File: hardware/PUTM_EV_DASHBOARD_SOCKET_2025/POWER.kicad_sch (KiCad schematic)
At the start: 10 parts, among them J4 Conn_01x01, J5 Conn_01x01, J5POWER1 Conn_01x06_MountingPin, J8 Conn_01x03_Socket, U1 SPX3819M5-L-5-0, U2 SPX3819M5-L-3-3

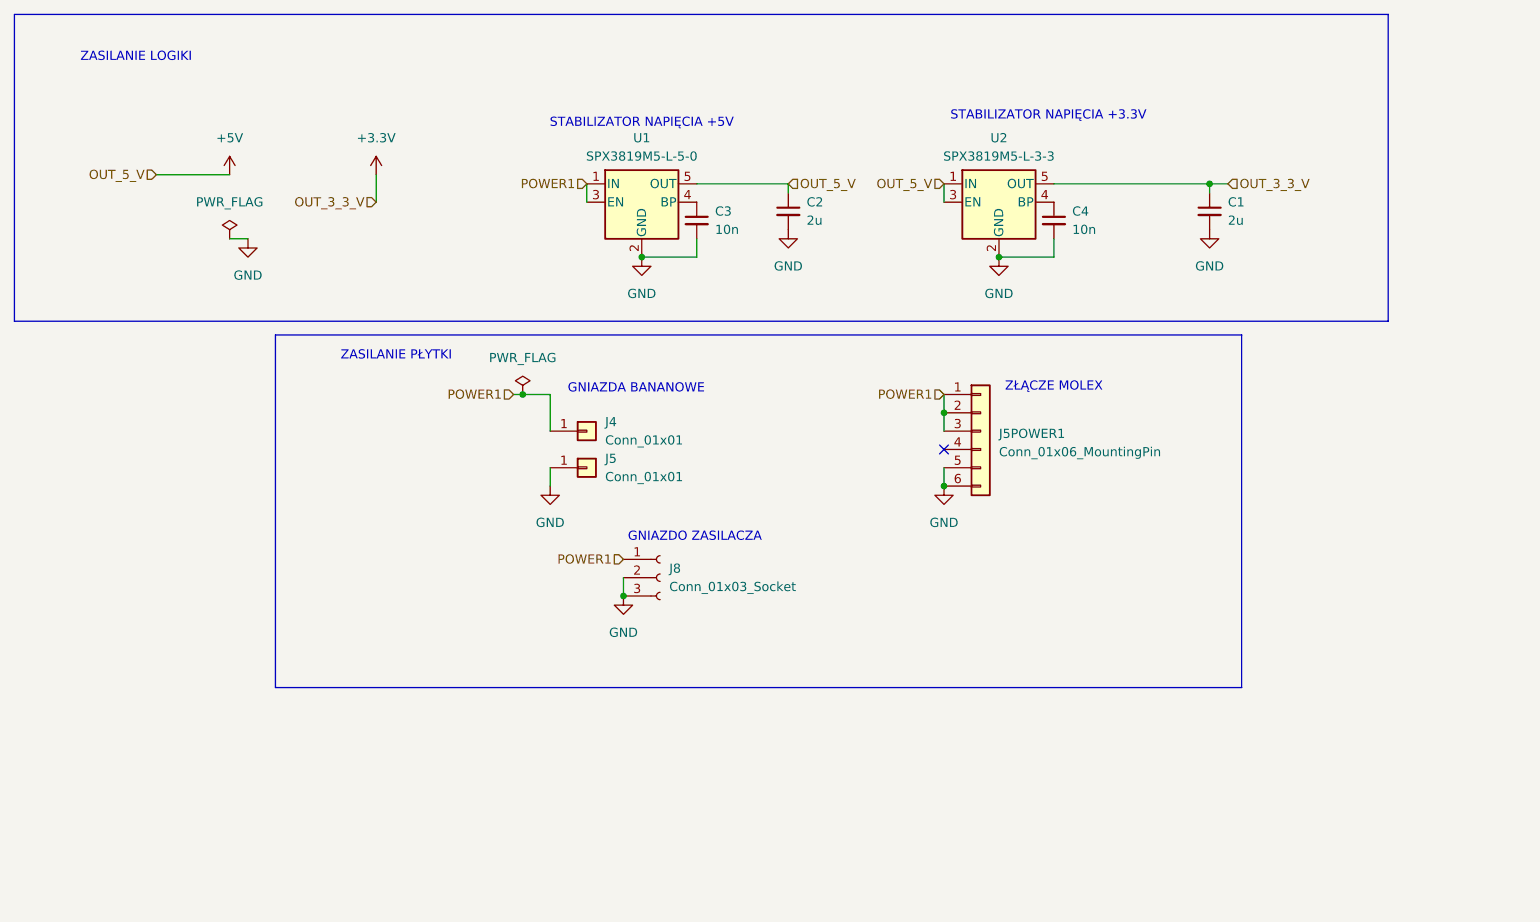
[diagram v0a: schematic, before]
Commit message: dodano łezki do pól smd, pola lutownicze do przelotek, dodano zabezpieczenie przed odwrotna polaryzacją, odsunięto ścieżki od krawędzi płytki, poprawiono can,
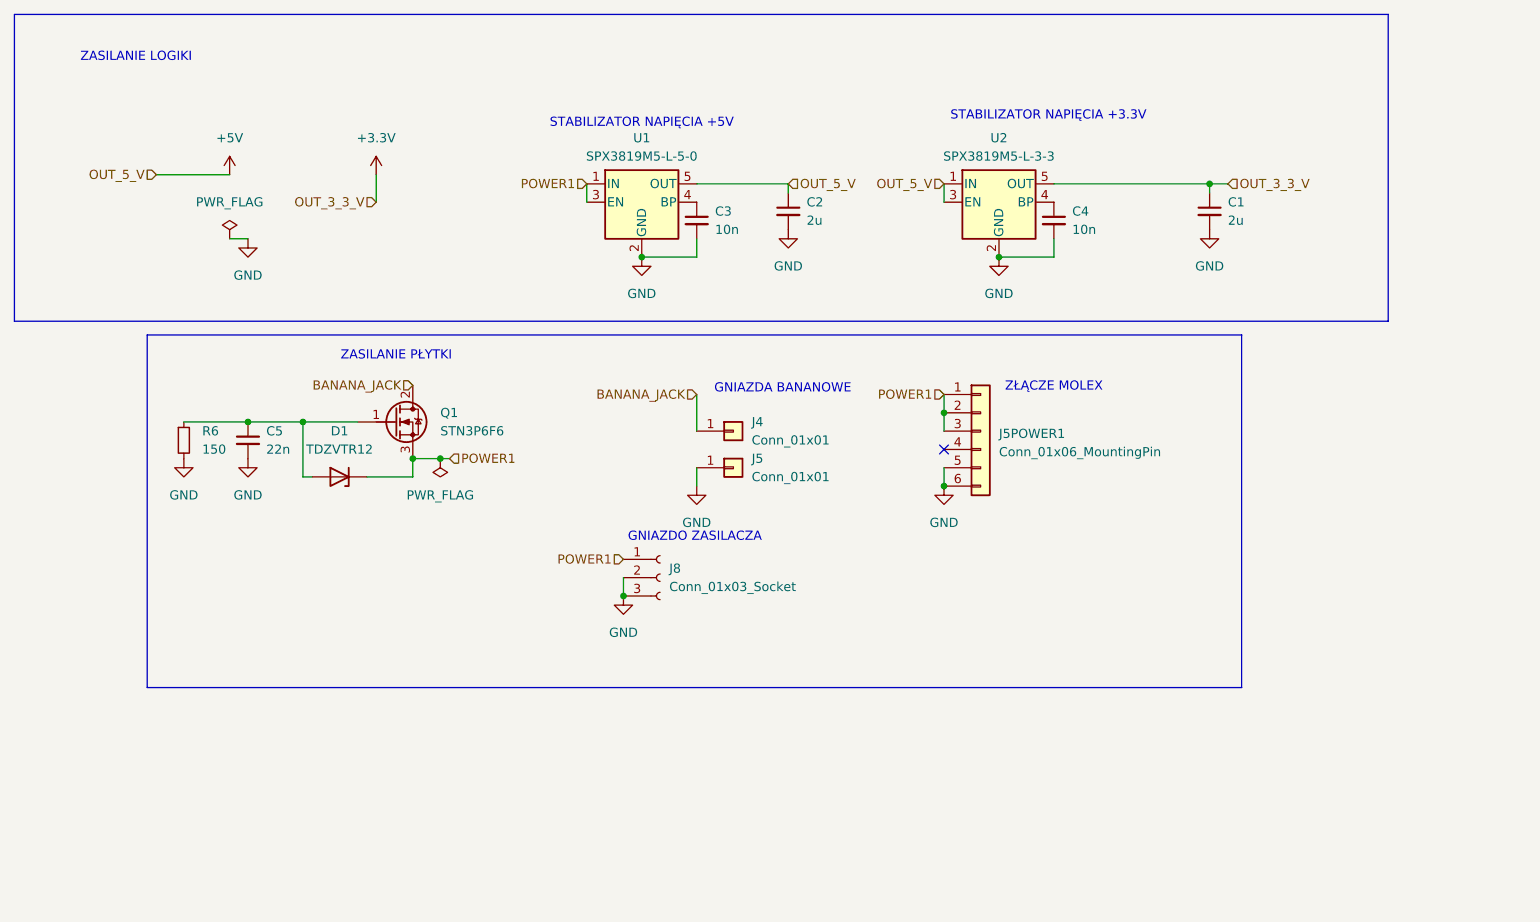
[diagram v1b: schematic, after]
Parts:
- added C5: 22n, Capacitor_SMD:C_0603_1608Metric, symbol Device:C_Small
- added D1: TDZVTR12, SamacSys_Parts:TDZVTR20, symbol Device:D_Zener
- added Q1: STN3P6F6, Package_TO_SOT_SMD:SOT-223-3_TabPin2, symbol Transistor_FET:BSP129
- added R6: 150, Resistor_SMD:R_1206_3216Metric, symbol Device:R_Small
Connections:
- net GND: now also C5.2, R6.2
- net POWER1: now also D1.1 (K), Q1.3 (S); no longer J4.1 (Pin_1)
- new net: C5.1, D1.2 (A), Q1.1 (G), R6.1
- new net BANANA_JACK: J4.1 (Pin_1), Q1.2 (D)
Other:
- moved on the sheet: J4, J5

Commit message: Bogracz Czas przygotowania: 3 godziny 30 minut Liczba porcji: 2100 g gulaszu  W 100 g dania: Wartość energetyczna 156 kcal Węglowodany 5 g - W tym cukry 2 g Białko 7 g Tłuszcze 12 g
Składniki

800 g mięsa wołowego - np. pręga oraz łopatka
200 g boczku gotowanego wędzonego
100 g dobrej jakosci słoniny
6 łyżek dobrej jakości smalcu - około 100 g
2 średniej wielkości cebule - około 330 g
2 średniej wielkości czerwone papryki - około 400 g
5 ząbków czosnku - około 25 g
500 g ziemniaków - można pominąć lub dać kluseczki
2 łyżki koncentratu pomidorowego - do 50 g
400 ml wody - trochę więcej niż 1,5 szklanki
zioła i przyprawy: 2 listki laurowe, 3 ziarna ziela angielskiego; 1 pełna łyżeczka słodkiej papryki; 1 płaska łyżeczka soli; po pół łyżeczki wędzonej i ostrej papryki; 1/3 łyżeczki czarnego pieprzu
Składniki:
Bogracz
Szklanka ma u mnie pojemność 250 ml.

Warzywa ważone były przed ewentualnym obraniem/przygotowaniem. Zawsze podaję wagę użytych przeze mnie warzyw lub owoców. Nie trzeba jednak stosować się do wytycznych co do grama. Wagi podawane są po to, by łatwiej Wam było zorientować się, jaka mniej więcej ilość potrzebna jest do zrobienia danego dania.

Kalorie policzone zostały na podstawie użytych przeze mnie składników. Jest to więc orientacyjna liczba kalorii, ponieważ Twoje składniki mogą mieć inną liczbę kalorii niż te, których użyłam ja. Z podanej ilości składników otrzymasz Bogracz o wadze około 2100 gramów. Zanim zaczniesz szykować ten gulasz, polecam najpierw przeczytać cały przepis, by przygotować się odpowiednio wcześniej do kolejnych etapów wykonania.

UWAGA: Bogracz, to rodzaj kociołka stalowego lub emaliowanego, który rozszerza się ku górze. Kociołek podwieszany jest na trójnogu i wieszany na metalowym łańcuchu. Bogracz wisi nad ogniskiem, a w środku gotuje się węgierski gulasz. Zaczęto zatem nazywać tak samo i danie. Ponieważ zdecydowana większość Czytelników nie ma możliwości szykowania tego gulaszu w kociołku na świeżym powietrzu, podaję przepis na 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
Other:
- note added: "ZABEZPIECZENIE PRZED ODWROTNĄ POLARYZACJĄ"
- moved on the sheet: C5, D1, Q1, R6
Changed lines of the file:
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@@
+		)
+	)
+	(text "ZABEZPIECZENIE PRZED ODWROTNĄ POLARYZACJĄ\n"
+		(exclude_from_sim no)
+		(at 82.55 72.644 0)
+		(effects
+			(font
+				(size 1.27 1.27)
+			)
 		)
 	)
@@
 	)
 	(junction
-		(at 92.71 77.47)
+		(at 93.98 87.63)
 		(diameter 0)
 		(color 0 0 0 0)
@@
 	)
 	(junction
-		(at 69.85 72.39)
+		(at 71.12 82.55)
 		(diameter 0)
 		(color 0 0 0 0)
@@
 	)
 	(junction
-		(at 77.47 72.39)
+		(at 78.74 82.55)
 		(diameter 0)
 		(color 0 0 0 0)
 	)
 	(junction
-		(at 96.52 77.47)
+		(at 97.79 87.63)
 		(diameter 0)
 		(color 0 0 0 0)
@@
 	(wire
 		(pts
-			(xy 77.47 72.39) (xy 85.09 72.39)
+			(xy 78.74 82.55) (xy 86.36 82.55)
 		)
 		(stroke
@@
 	(wire
 		(pts
-			(xy 77.47 80.01) (xy 77.47 72.39)
+			(xy 78.74 90.17) (xy 78.74 82.55)
 		)
 		(stroke
@@
 	(wire
 		(pts
-			(xy 92.71 80.01) (xy 92.71 77.47)
+			(xy 93.98 90.17) (xy 93.98 87.63)
 		)
 		(stroke
@@
 	(wire
 		(pts
-			(xy 97.79 77.47) (xy 96.52 77.47)
+			(xy 99.06 87.63) (xy 97.79 87.63)
 		)
 		(stroke
@@
 	(wire
 		(pts
-			(xy 96.52 77.47) (xy 92.71 77.47)
+			(xy 97.79 87.63) (xy 93.98 87.63)
 		)
 		(stroke
@@
 	(wire
 		(pts
-			(xy 69.85 72.39) (xy 77.47 72.39)
+			(xy 71.12 82.55) (xy 78.74 82.55)
 		)
 		(stroke
@@
 	(wire
 		(pts
-			(xy 86.36 80.01) (xy 92.71 80.01)
+			(xy 87.63 90.17) (xy 93.98 90.17)
 		)
 		(stroke
@@
 	(wire
 		(pts
-			(xy 78.74 80.01) (xy 77.47 80.01)
+			(xy 80.01 90.17) (xy 78.74 90.17)
 		)
 		(stroke
@@
 	(wire
 		(pts
-			(xy 60.96 72.39) (xy 69.85 72.39)
+			(xy 62.23 82.55) (xy 71.12 82.55)
 		)
 		(stroke
@@
 	(hierarchical_label "BANANA_JACK"
 		(shape input)
-		(at 92.71 67.31 180)
+		(at 93.98 77.47 180)
 		(effects
 			(font
@@
 	(hierarchical_label "POWER1"
 		(shape input)
-		(at 97.79 77.47 0)
+		(at 99.06 87.63 0)
 		(effects
 			(font
@@
 	(symbol
 		(lib_id "Device:C_Small")
-		(at 69.85 74.93 0)
+		(at 71.12 85.09 0)
 		(unit 1)
 		(exclude_from_sim no)
@@
 		(fields_autoplaced yes)
 		(property "Reference" "C5"
-			(at 72.39 73.6662 0)
+			(at 73.66 83.8262 0)
 			(effects
 				(font
@@
 		)
 		(property "Value" "22n"
-			(at 72.39 76.2062 0)
+			(at 73.66 86.3662 0)
 			(effects
 				(font
@@
 		)
 		(property "Footprint" "Capacitor_SMD:C_0603_1608Metric"
-			(at 69.85 74.93 0)
+			(at 71.12 85.09 0)
 			(effects
 				(font
@@
 		)
 		(property "Datasheet" "~"
-			(at 69.85 74.93 0)
+			(at 71.12 85.09 0)
 			(effects
 				(font
@@
 		)
 		(property "Description" "Unpolarized capacitor, small symbol"
-			(at 69.85 74.93 0)
+			(at 71.12 85.09 0)
 			(effects
 				(font
@@
 	(symbol
 		(lib_id "Device:R_Small")
-		(at 60.96 74.93 0)
+		(at 62.23 85.09 0)
 		(unit 1)
 		(exclude_from_sim no)
@@
 		(dnp no)
 		(property "Reference" "R6"
-			(at 63.5 73.6599 0)
+			(at 64.77 83.8199 0)
 			(effects
 				(font
@@
 		)
 		(property "Value" "150"
-			(at 63.5 76.1999 0)
+			(at 64.77 86.3599 0)
 			(effects
 				(font
@@
 		)
 		(property "Footprint" "Resistor_SMD:R_1206_3216Metric"
-			(at 60.96 74.93 0)
+			(at 62.23 85.09 0)
 			(effects
 				(font
@@
 		)
 		(property "Datasheet" "~"
-			(at 60.96 74.93 0)
+			(at 62.23 85.09 0)
 			(effects
 				(font
@@
 		)
 		(property "Description" "Resistor, small symbol"
-			(at 60.96 74.93 0)
+			(at 62.23 85.09 0)
 			(effects
 				(font
@@
 	(symbol
 		(lib_id "Device:D_Zener")
-		(at 82.55 80.01 180)
+		(at 83.82 90.17 180)
 		(unit 1)
 		(exclude_from_sim no)
@@
 		(dnp no)
 		(property "Reference" "D1"
-			(at 82.55 73.66 0)
+			(at 83.82 83.82 0)
 			(effects
 				(font
@@
 		)
 		(property "Value" "TDZVTR12"
-			(at 82.55 76.2 0)
+			(at 83.82 86.36 0)
 			(effects
 				(font
@@
 		)
 		(property "Footprint" "SamacSys_Parts:TDZVTR20"
-			(at 82.55 80.01 0)
+			(at 83.82 90.17 0)
 			(effects
 				(font
@@
 		)
 		(property "Datasheet" "https://www.mouser.pl/ProductDetail/ROHM-Semiconductor/TDZVTR12?qs=4v%252BiZTmLVHH4uFenhw55Ug%3D%3D"
-			(at 82.55 80.01 0)
+			(at 83.82 90.17 0)
 			(effects
 				(font
@@
 		)
 		(property "Description" "Zener diode"
-			(at 82.55 80.01 0)
+			(at 83.82 90.17 0)
 			(effects
 				(font
@@
 	(symbol
 		(lib_id "Transistor_FET:BSP129")
-		(at 90.17 72.39 0)
+		(at 91.44 82.55 0)
 		(unit 1)
 		(exclude_from_sim no)
@@
 		(fields_autoplaced yes)
 		(property "Reference" "Q1"
-			(at 96.52 71.1199 0)
+			(at 97.79 81.2799 0)
 			(effects
 				(font
@@
 		)
 		(property "Value" "STN3P6F6"
-			(at 96.52 73.6599 0)
+			(at 97.79 83.8199 0)
 			(effects
 				(font
@@
 		)
 		(property "Footprint" "Package_TO_SOT_SMD:SOT-223-3_TabPin2"
-			(at 95.25 74.295 0)
+			(at 96.52 84.455 0)
 			(effects
 				(font
@@
 		)
 		(property "Datasheet" "https://www.mouser.pl/ProductDetail/STMicroelectronics/STN3P6F6?qs=uZT4uyn3SpyqV6vypo4MhA%3D%3D"
-			(at 95.25 76.2 0)
+			(at 96.52 86.36 0)
 			(effects
 				(font
@@
 		)
 		(property "Description" "0.35A Id, 240V Vds, N-Channel MOSFET, SOT-223"
-			(at 90.17 72.39 0)
+			(at 91.44 82.55 0)
 			(effects
 				(font
@@
 	(symbol
 		(lib_id "power:GND")
-		(at 69.85 77.47 0)
+		(at 71.12 87.63 0)
 		(unit 1)
 		(exclude_from_sim no)
@@
 		(fields_autoplaced yes)
 		(property "Reference" "#PWR044"
-			(at 69.85 83.82 0)
+			(at 71.12 93.98 0)
 			(effects
 				(font
@@
 		)
 		(property "Value" "GND"
-			(at 69.85 82.55 0)
+			(at 71.12 92.71 0)
 			(effects
 				(font
@@
 		)
 		(property "Footprint" ""
-			(at 69.85 77.47 0)
+			(at 71.12 87.63 0)
 			(effects
 				(font
@@
 		)
 		(property "Datasheet" ""
-			(at 69.85 77.47 0)
+			(at 71.12 87.63 0)
 			(effects
 				(font
@@
 		)
 		(property "Description" "Power symbol creates a global label with name \"GND\" , ground"
-			(at 69.85 77.47 0)
+			(at 71.12 87.63 0)
 			(effects
 				(font
@@
 	(symbol
 		(lib_id "power:GND")
-		(at 60.96 77.47 0)
+		(at 62.23 87.63 0)
 		(unit 1)
 		(exclude_from_sim no)
@@
 		(fields_autoplaced yes)
 		(property "Reference" "#PWR042"
-			(at 60.96 83.82 0)
+			(at 62.23 93.98 0)
 			(effects
 				(font
@@
 		)
 		(property "Value" "GND"
-			(at 60.96 82.55 0)
+			(at 62.23 92.71 0)
 			(effects
 				(font
@@
 		)
 		(property "Footprint" ""
-			(at 60.96 77.47 0)
+			(at 62.23 87.63 0)
 			(effects
 				(font
@@
 		)
 		(property "Datasheet" ""
-			(at 60.96 77.47 0)
+			(at 62.23 87.63 0)
 			(effects
 				(font
@@
 		)
 		(property "Description" "Power symbol creates a global label with name \"GND\" , ground"
-			(at 60.96 77.47 0)
+			(at 62.23 87.63 0)
 			(effects
 				(font
@@
 	(symbol
 		(lib_id "power:PWR_FLAG")
-		(at 96.52 77.47 180)
+		(at 97.79 87.63 180)
 		(unit 1)
 		(exclude_from_sim no)
@@
 		(fields_autoplaced yes)
 		(property "Reference" "#FLG01"
-			(at 96.52 79.375 0)
+			(at 97.79 89.535 0)
 			(effects
 				(font
@@
 		)
 		(property "Value" "PWR_FLAG"
-			(at 96.52 82.55 0)
+			(at 97.79 92.71 0)
 			(effects
 				(font
@@
 		)
 		(property "Footprint" ""
-			(at 96.52 77.47 0)
+			(at 97.79 87.63 0)
 			(effects
 				(font
@@
 		)
 		(property "Datasheet" "~"
-			(at 96.52 77.47 0)
+			(at 97.79 87.63 0)
 			(effects
 				(font
@@
 		)
 		(property "Description" "Special symbol for telling ERC where power comes from"
-			(at 96.52 77.47 0)
-			(effects
-				(font
+			(at 97.79 87.63 0)
+			(effects
+				(font

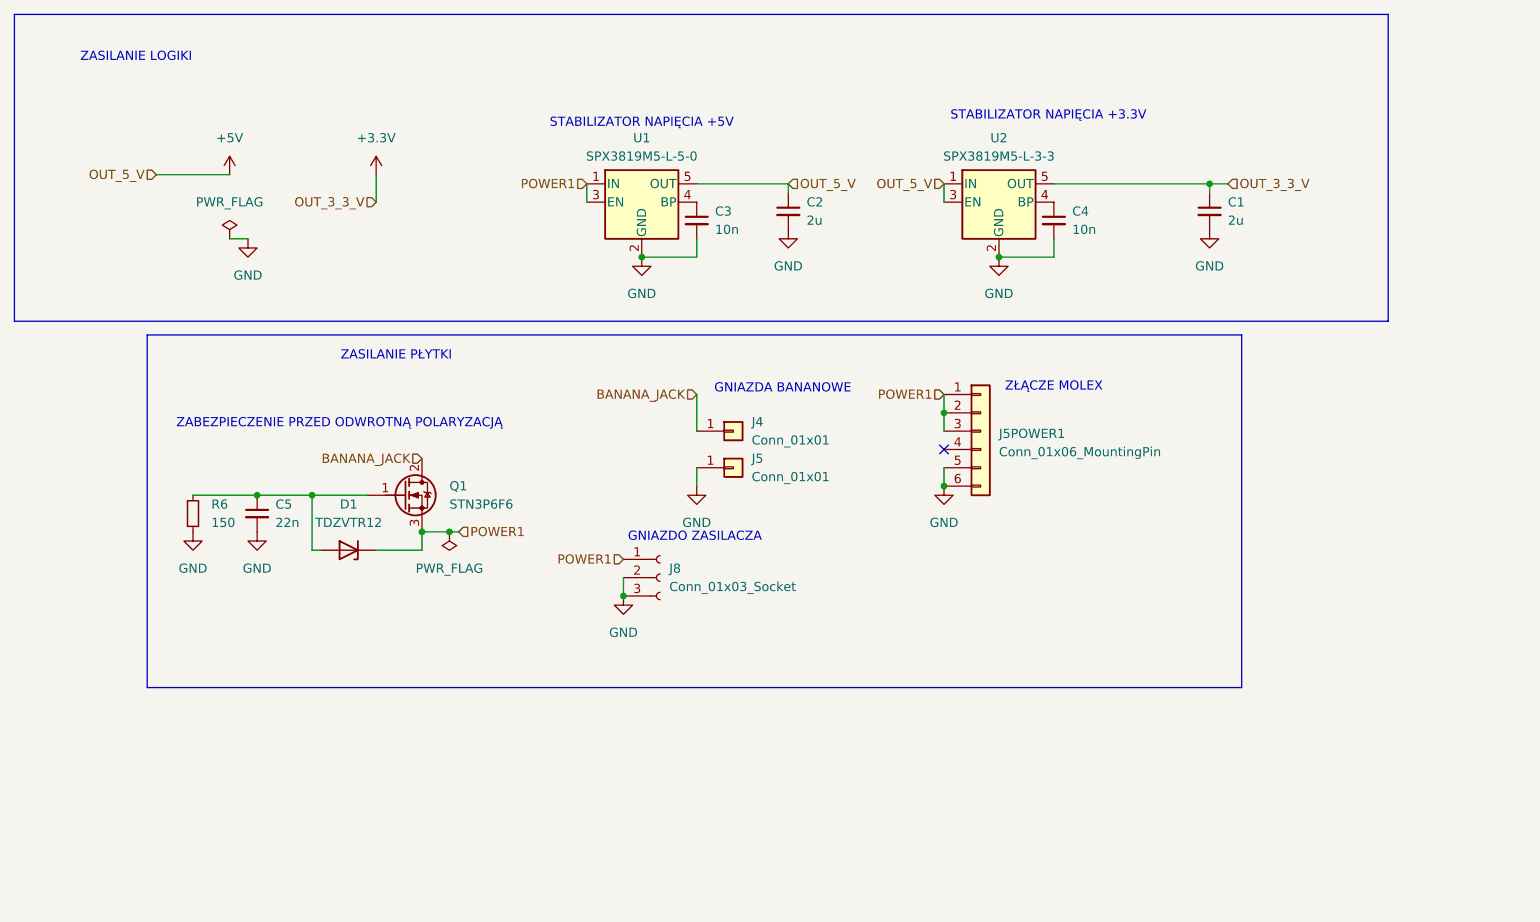
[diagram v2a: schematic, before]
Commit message: fixed button logic, holes for inserts, distance from mounting holes to P4 socket, changed jumpers, TVS diode and footprint for laboratory socket 4m
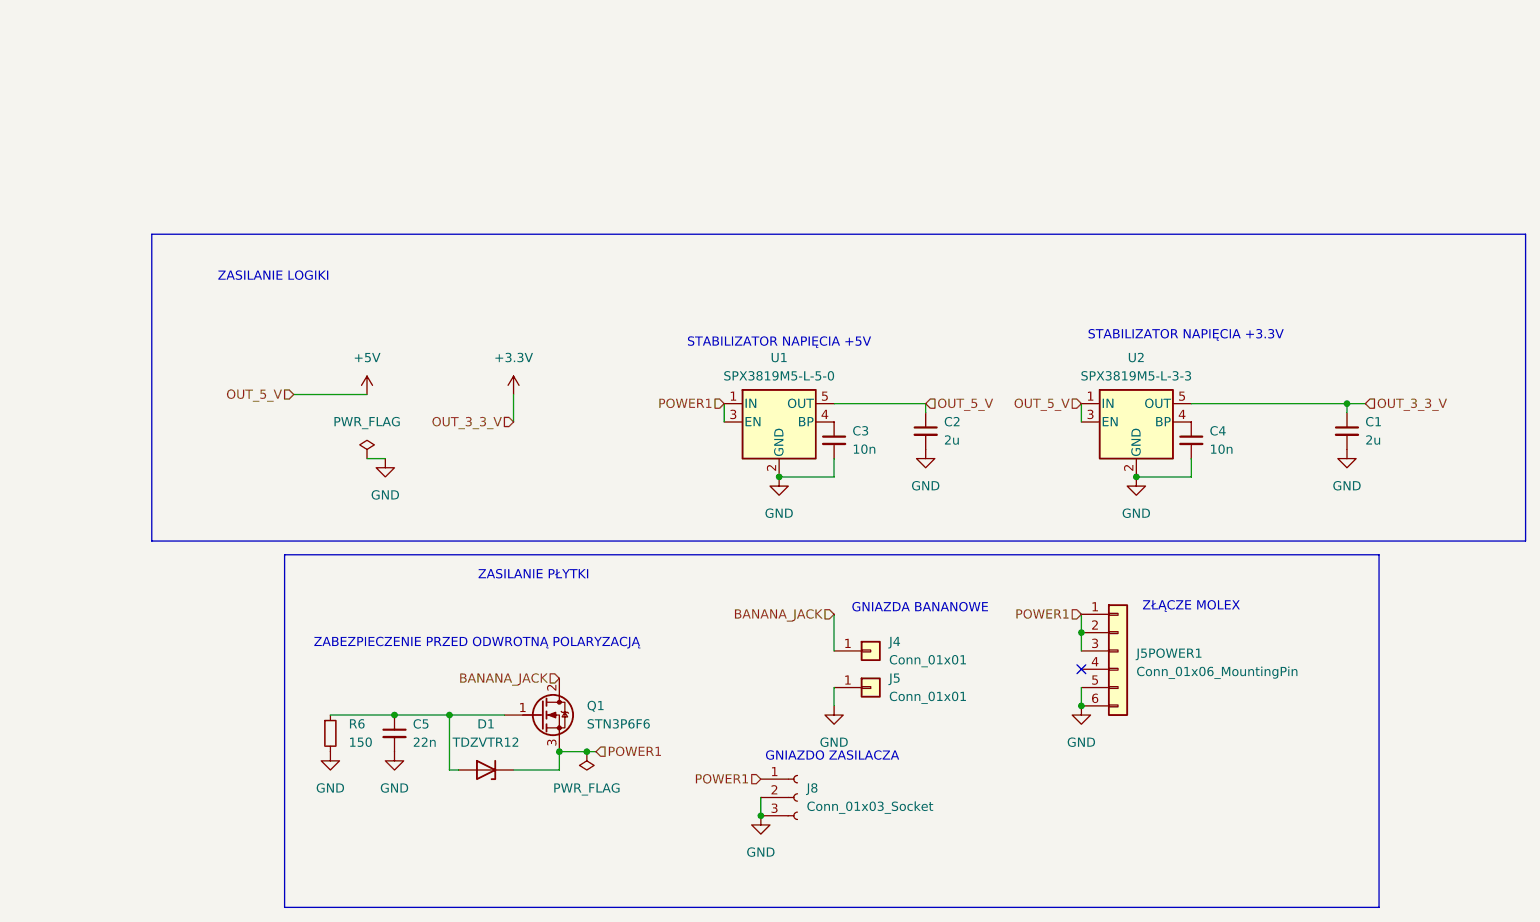
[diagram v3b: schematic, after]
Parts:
- J4, J5: footprint footprints:PJ3253 -> footprints:D-3230
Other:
- moved on the sheet: C1, C2, C3, C4, C5, D1, J4, J5, J5POWER1, J8, Q1, R6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
